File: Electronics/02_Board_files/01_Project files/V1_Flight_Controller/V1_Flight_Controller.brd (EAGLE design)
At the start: 46.2 x 46.2 mm, 3 parts, among them U1 STM32F030K6T6, U2 MPU-6050

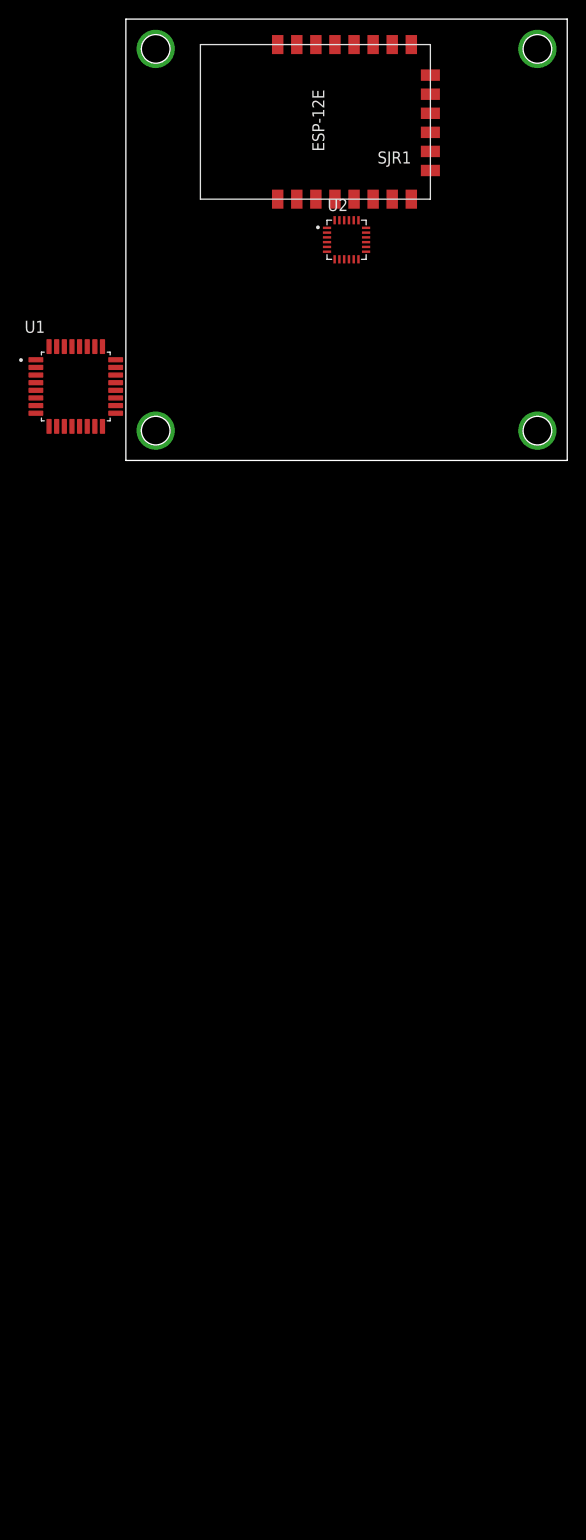
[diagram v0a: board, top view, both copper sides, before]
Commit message: Schematic changes
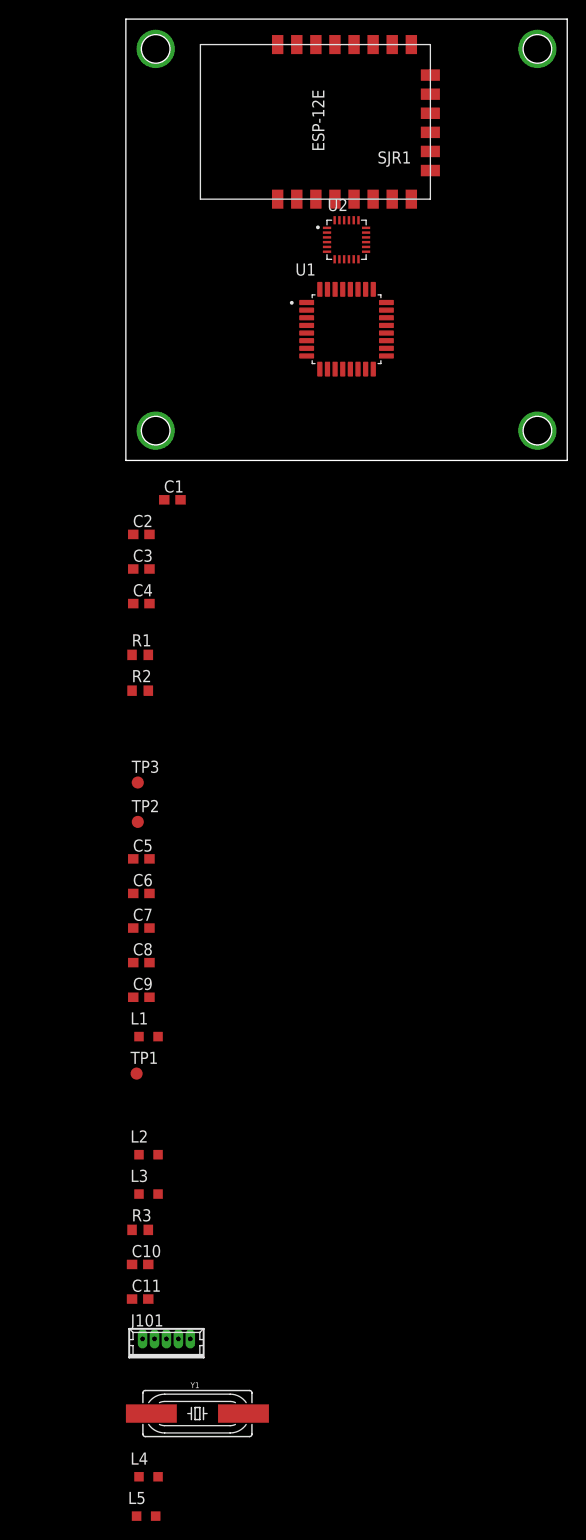
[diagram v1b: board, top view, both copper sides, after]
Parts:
- added C1: 0.1uF, 2V, ±10%, adafruit:C0603
- added C10, C11, C5, C6, C7, C8, C9: (no value), adafruit:C0603
- added C2: 0.1uF, 4V, ±10%, adafruit:C0603
- added C3: 2.2nF, 50V, ±10%, adafruit:C0603
- added C4: 10nF, 4V, ±10%, adafruit:C0603
- added J101: JTAG_CONNECTOR, con-molex:53047-05
- added L1, L2, L3, L4, L5: (no value), rcl:L2012C
- added R1, R2: 4.7k, adafruit:R0603
- added R3: (no value), adafruit:R0603
- added TP1, TP2, TP3: TPB1,27, testpad:B1,27
- added Y1: 8MHz, SparkFun-Clocks:HC49UP
- moved U1 29.0 mm to (23.1, 13.8)
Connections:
- net TIM1_CH1 renamed PWM_PIN1
- net TIM1_CH2 renamed PWM_PIN2
- net TIM1_CH3 renamed PWM_PIN3
- net TIM1_CH4 renamed PWM_PIN4
- new net 3V3_IMU: C2.1, C4.1, L5.1, R1.1, R2.1, U2.13, U2.8
- new net 3V3_MCU: C7.1, C8.1, C9.1, J101.1, L1.1, L2.2, L4.1, R3.1, TP1.TP, U1.1, U1.17
- new net GND_IMU: C1.2, C2.2, C3.2, C4.2, U2.1, U2.11, U2.18, U2.9
- new net GND_MCU: C10.2, C11.2, C5.2, C6.2, C7.2, C8.2, C9.2, J101.3, L3.2, U1.16, U1.32
- new net I2C1_SCL: TP2.TP, U1.29
- new net I2C1_SDA: TP3.TP, U1.30
- new net IMU_INT: U2.12
- new net N$1: C1.1, U2.10
- new net N$2: C3.1, U2.20
- new net SWCLK: J101.2, U1.24
- new net SWDIO: J101.4, U1.23
- new net USART1_RX: U1.9
- new net USART1_TX: U1.8
- new net VBAT_LEVEL: U1.6
- new net VDDA: C5.1, C6.1, L1.2, U1.5
- net 3V3: now also L4.2, L5.2; no longer U1.1, U1.17, U1.5, U2.13, U2.8
- net BOOT0: now also L2.1, L3.1
- net GND: no longer U1.16, U1.32, U2.18
- net NRST: now also J101.5, R3.2
- net SCL: now also R1.2
- net SDA: now also R2.2
- net XTAL_IN: now also C10.1, Y1.1
- net XTAL_OUT: now also C11.1, Y1.2

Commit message: added sheets for power section and motor driver
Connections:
- new net RST: SJR1.1
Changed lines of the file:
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@@
 <wire x1="2.475" y1="-15" x2="2.475" y2="-11.375" width="0" layer="19" extent="1-1"/>
+</signal>
+<signal name="RST">
+<contactref element="SJR1" pad="1"/>
 </signal>
 </signals>
